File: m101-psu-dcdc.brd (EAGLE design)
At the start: 100 x 50 mm, 39 parts, among them U1 FX2-20P-1.27DS, U2 SHHN000A3CL41Z, U3 G3VM-62C1, U4 ERM1-5MM, U5 SCREW-M2X8, U6 SCREW-M2X8, U7 NUT-M2-SELFLOCK, U8 NUT-M2-SELFLOCK

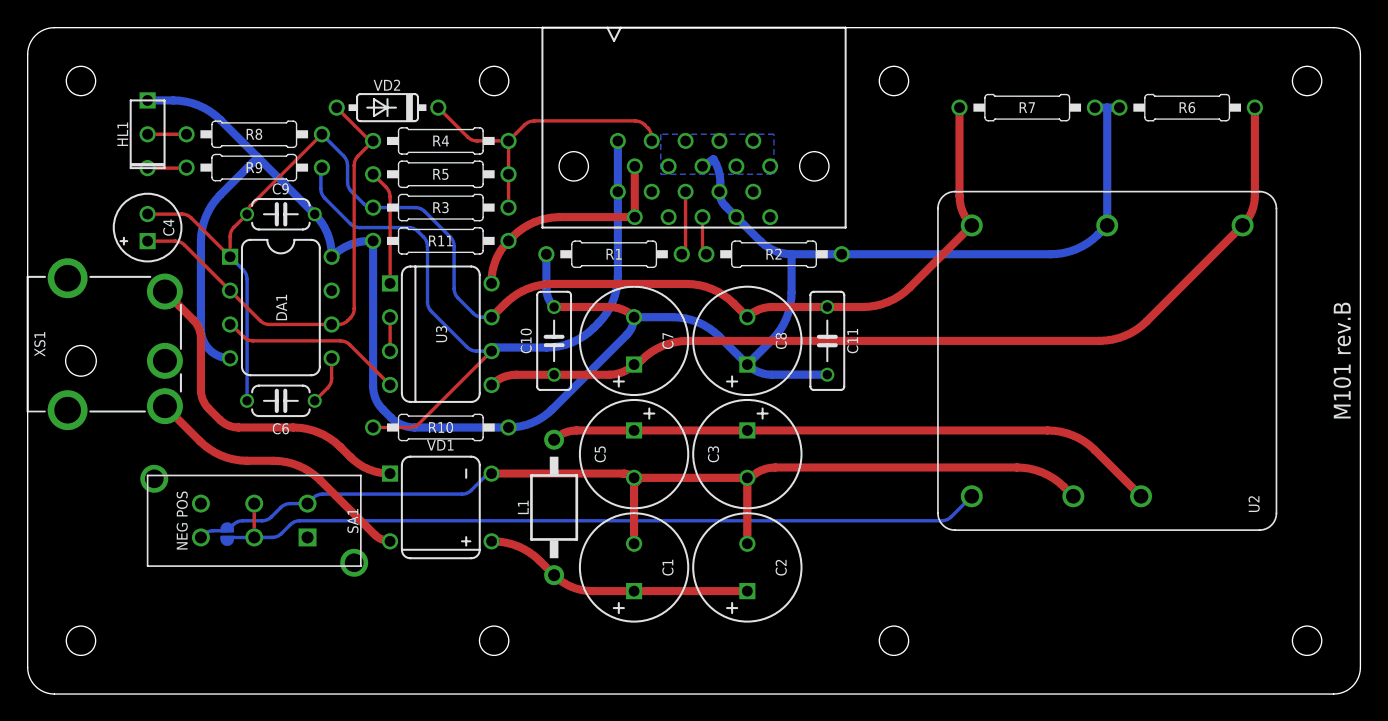
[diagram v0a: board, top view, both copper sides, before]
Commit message: M101 rev.C Initial Schematic
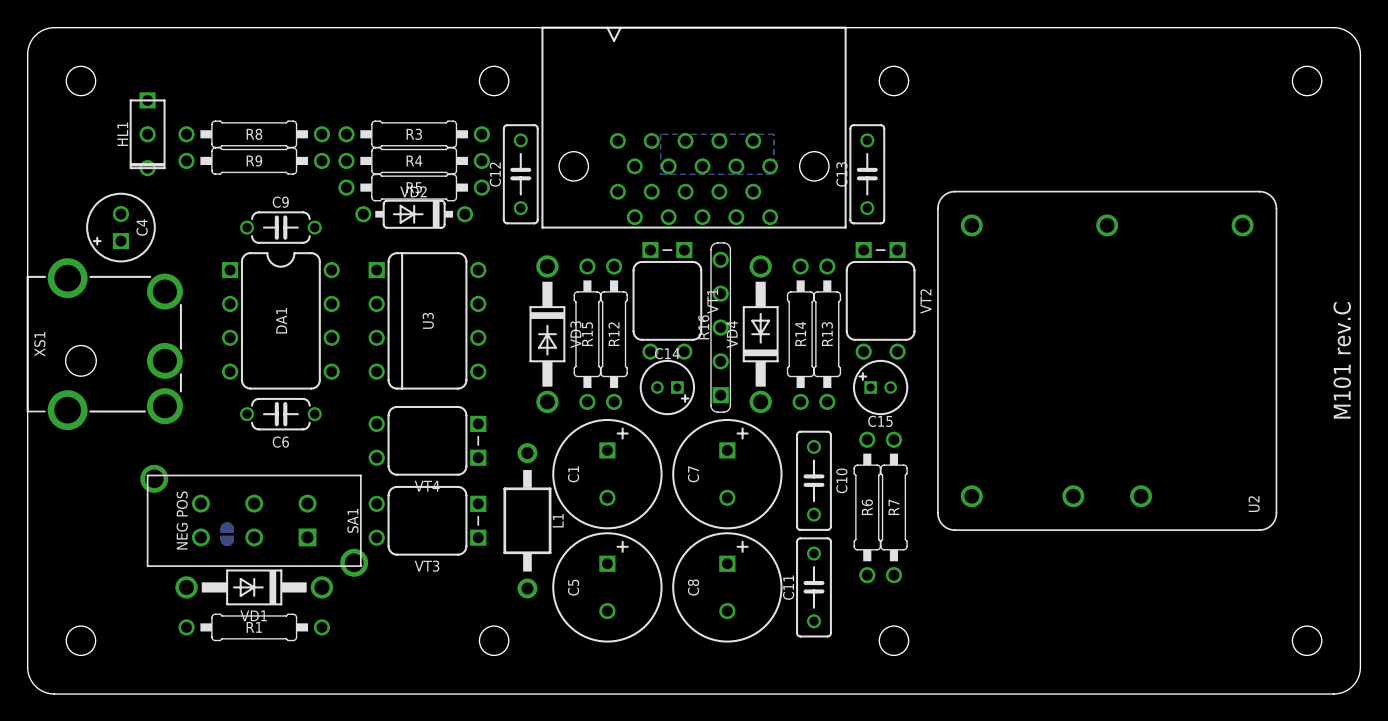
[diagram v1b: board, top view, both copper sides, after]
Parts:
- removed C2, C3: 33U/50V, capacitors-electrolytic:E3,5-8
- removed R10, R11, R2: 100K(TH), resistors:R-0207/10
- added C12, C13: 22N(FILM), capacitors:C050-025X075
- added C14, C15: 1U/50V, capacitors-electrolytic:E1,5-4
- added R12, R13: 100R(TH), resistors:R-0207/10
- added R14, R15: 220K(TH), resistors:R-0207/10
- added R16: 100K*4(SIL5), resistors:R-SIL5
- added VD3, VD4: 10V(1N4740), diodes-zener:DO41-10
- added VT1: IRFD9024, transistors-fet:HVMDIP-4
- added VT2, VT3, VT4: IRFD014, transistors-fet:HVMDIP-4
- PCB1: value M101 rev.B -> M101 rev.C
- R1: value 100K(TH) -> 22K(TH)
- VD1: value DF01M -> 10V(1N4740); device diodes:MDIP-4 -> diodes-zener:DO41-10
- moved R1 38.9 mm to (17.0, 5.00), turned to 0 degrees
- moved R6 38.4 mm to (63.0, 14.0), turned to 90 degrees
- moved R7 31.6 mm to (65.0, 14.0), turned to 90 degrees
- moved C10 22.1 mm to (59.0, 16.0), turned to 90 degrees
- moved C8 18.6 mm to (52.5, 8.00), turned to 270 degrees
- moved C11 18.5 mm to (59.0, 8.00), turned to 90 degrees
- moved VD1 15.2 mm to (17.0, 8.00), turned to 180 degrees
- moved C7 12.2 mm to (52.5, 16.5), turned to 270 degrees
- moved C5 10.2 mm to (43.5, 8.00)
- moved VD2 8.25 mm to (29.0, 36.0)
- moved C1 7.28 mm to (43.5, 16.5), turned to 270 degrees
- moved R3 5.85 mm to (29.0, 42.0)
- moved R4 2.50 mm to (29.0, 40.0)
- moved L1 2.24 mm to (37.5, 13.0), turned to 270 degrees
- moved R5 2.24 mm to (29.0, 38.0)
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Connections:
- removed net N$2: VD1.1, XS1.3
- new net N$17: C14.-, R12.1, R15.1, VD3.A, VT1.3
- new net N$18: C12.2, PCB1.A+15', PCB1.B+15', VT1.1, VT1.2
- new net N$19: C12.1, R12.2
- new net N$21: C13.1, PCB1.A-15', PCB1.B-15', VT2.1, VT2.2
- new net N$23: C13.2, R13.2
- new net N$24: C15.+, R13.1, R14.1, VD4.C, VT2.3
- new net N$25: C15.-, R16.3, U3.8, VD4.A, VT2.4
- net GND: now also R14.2, R15.2, R16.1; no longer R1.2, R10.1, R11.2, R2.2
- net N$11: now also C14.+, R16.2, R9.2, U3.6, VD3.C, VT1.4; no longer VD1.2, XS1.1
- net N$12: now also R1.2, VD1.C, VT3.3, VT4.3; no longer PCB1.A-15', PCB1.B-15', R11.1, U3.8
- net N$20: now also R1.1, XS1.3; no longer C2.+, VD1.3
- net N$22: no longer C3.+
- net N$3: now also VD1.A, VT3.1, VT3.2, VT4.1, VT4.2; no longer C2.-, C3.-, VD1.4
- net N$4: now also R16.4; no longer R1.1
- net N$5: now also R16.5; no longer R2.1
- net N$8: now also VT3.4, VT4.4, XS1.1; no longer PCB1.A+15', PCB1.B+15', R10.2, R9.2, U3.6
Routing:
- net GND: track 156.8 -> 0.00 mm
- net -15V: track 101.0 -> 0.00 mm
- net N$3: track 78.0 -> 0.00 mm
- net N$15: track 69.3 -> 0.00 mm
- net N$16: track 59.5 -> 0.00 mm
- net N$8: track 56.0 -> 0.00 mm
- net N$22: track 45.9 -> 0.00 mm
- net N$10: track 35.4 -> 0.00 mm
- net N$2: track 24.8 -> 0.00 mm
- net SENSE: track 23.4 -> 0.00 mm
- net N$11: track 20.4 -> 0.00 mm
- net N$20: track 20.2 -> 0.00 mm
- net N$12: track 17.2 -> 0.00 mm
- net N$7: track 13.8 -> 0.00 mm
- net N$1: track 8.65 -> 0.00 mm
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
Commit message: M101 Parts renumbering
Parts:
- removed C14, C15: 1U/50V, capacitors-electrolytic:E1,5-4
- added C2: 10U/35V, capacitors-electrolytic:E2-5
- added C3: 33U/50V, capacitors-electrolytic:E3,5-8
- C10, C11: value 100N(FILM) -> 1U/50V; device capacitors:C050-025X075 -> capacitors-electrolytic:E1,5-4
- C4: value 10U/35V -> 100N(TH); device capacitors-electrolytic:E2-5 -> capacitors:C050-024X044
- C5: value 33U/50V -> 39U/35V
- C6: value 100N(TH) -> 39U/35V; device capacitors:C050-024X044 -> capacitors-electrolytic:E3,5-8
- C7: value 39U/35V -> 100N(TH); device capacitors-electrolytic:E3,5-8 -> capacitors:C050-024X044
- C8: value 39U/35V -> 100N(FILM); device capacitors-electrolytic:E3,5-8 -> capacitors:C050-025X075
- C9: value 100N(TH) -> 100N(FILM); device capacitors:C050-024X044 -> capacitors:C050-025X075
- U1: value FX2-20P-1.27DS -> SCREW-M2X8
- U2: value SHHN000A3CL41Z -> SCREW-M2X8; device regulators-switch-mode:DC/DC-C1 -> hardware:EMPTY
- U3: value G3VM-62C1 -> NUT-M2-SELFLOCK; device optoelectronics:DIL08 -> hardware:EMPTY
- U4: value ERM1-5MM -> NUT-M2-SELFLOCK
- U5: value SCREW-M2X8 -> FX2-20P-1.27DS
- U6: value SCREW-M2X8 -> SHHN000A3CL41Z; device hardware:EMPTY -> regulators-switch-mode:DC/DC-C1
- U7: value NUT-M2-SELFLOCK -> G3VM-62C1; device hardware:EMPTY -> optoelectronics:DIL08
- U8: value NUT-M2-SELFLOCK -> ERM1-5MM
- VT1: value IRFD9024 -> IRFD014
- VT3: value IRFD014 -> IRFD9024
- moved U2 210.1 mm to (-84.0, -105.0), turned to 0 degrees
- moved U6 210.1 mm to (81.0, 25.0), turned to 90 degrees
- moved U3 177.3 mm to (-85.0, -107.0), turned to 0 degrees
- moved U7 177.3 mm to (30.0, 28.0), turned to 270 degrees
- moved C9 48.3 mm to (59.0, 8.00), turned to 90 degrees
- moved C7 38.3 mm to (19.0, 35.0), turned to 0 degrees
- moved VT2 37.8 mm to (30.0, 13.0), turned to 90 degrees
- moved C6 35.9 mm to (52.5, 8.00), turned to 270 degrees
- moved VT4 35.6 mm to (64.0, 29.5), turned to 180 degrees
- moved VT3 24.4 mm to (48.0, 29.5), turned to 180 degrees
- moved VT1 20.8 mm to (30.0, 19.0), turned to 90 degrees
- moved C4 18.4 mm to (19.0, 21.0), turned to 0 degrees
- moved C11 15.8 mm to (64.0, 23.0), turned to 0 degrees
- moved C10 13.0 mm to (48.0, 23.0), turned to 180 degrees
- moved C5 12.4 mm to (52.5, 16.5)
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- renumbered R14 to R11, R15 to R10, R16 to R2
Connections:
- net -15V: now also C2.-, C4.1, C6.-, C7.1, U6.6, U7.7; no longer C11.1, C4.-, C6.1, C8.-, U2.6, U3.7
- net GND: now also C5.-, C6.+, C7.2, C8.1, U6.5; no longer C10.1, C11.2, C7.-, C8.+, U2.5
- net N$1: now also U7.1; no longer U3.1
- net N$10: now also C2.+; no longer C4.+
- net N$11: now also C10.+, U7.6, VT3.4; no longer C14.+, U3.6, VT1.4
- net N$12: now also VT1.3, VT2.3; no longer VT3.3, VT4.3
- net N$15: now also C5.+, C8.2, U6.4, U7.5; no longer C10.2, C7.+, U2.4, U3.5
- net N$16: now also U6.3; no longer U2.3
- net N$17: now also C10.-, VT3.3; no longer C14.-, VT1.3
- net N$18: now also VT3.1, VT3.2; no longer VT1.1, VT1.2
- net N$21: now also VT4.1, VT4.2; no longer VT2.1, VT2.2
- net N$22: now also C3.+, U6.1; no longer C5.+, U2.1
- net N$24: now also C11.+, VT4.3; no longer C15.+, VT2.3
- net N$25: now also C11.-, U7.8, VT4.4; no longer C15.-, U3.8, VT2.4
- net N$3: now also C3.-, U6.2, VT1.1, VT1.2, VT2.1, VT2.2; no longer C5.-, U2.2, VT3.1, VT3.2, VT4.1, VT4.2
- net N$6: now also C4.2; no longer C6.2
- net N$7: now also U7.4; no longer U3.4
- net N$8: now also VT1.4, VT2.4; no longer VT3.4, VT4.4
- net N$9: now also U7.2, U7.3; no longer U3.2, U3.3

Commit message: M101 Polarity Protection Fix
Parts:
- turned VT1 to 270 degrees
- turned VT2 to 270 degrees
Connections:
- net N$3: now also VT1.4, VT2.4; no longer VT1.1, VT1.2, VT2.1, VT2.2
- net N$8: now also VT1.1, VT1.2, VT2.1, VT2.2; no longer VT1.4, VT2.4
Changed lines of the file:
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@@
 <?xml version="1.0" encoding="utf-8"?>
 <!DOCTYPE eagle SYSTEM "eagle.dtd">
-<eagle version="7.5.4">
+<eagle version="7.6.0">
 <drawing>
 <settings>
@@
 <attribute name="MOUSER" value="652-4605X-1LF-100K" x="52" y="27.5" size="1.778" layer="27" rot="R90" display="off"/>
 </element>
-<element name="VT2" library="transistors-fet" package="HVMDIP-4" value="IRFD014" x="30" y="13" rot="R90"/>
-<element name="VT1" library="transistors-fet" package="HVMDIP-4" value="IRFD014" x="30" y="19" rot="R90"/>
+<element name="VT2" library="transistors-fet" package="HVMDIP-4" value="IRFD014" x="30" y="13" rot="R270"/>
+<element name="VT1" library="transistors-fet" package="HVMDIP-4" value="IRFD014" x="30" y="19" rot="R270"/>
 <element name="VD1" library="diodes-zener" package="DO41-10" value="10V(1N4740)" x="17" y="8" rot="R180"/>
 <element name="R1" library="resistors" package="R-0207/10" value="22K(TH)" x="17" y="5">
@@
 <contactref element="C1" pad="-"/>
 <contactref element="S1" pad="1"/>
-<contactref element="VT2" pad="1"/>
-<contactref element="VT2" pad="2"/>
-<contactref element="VT1" pad="1"/>
-<contactref element="VT1" pad="2"/>
 <contactref element="VD1" pad="A"/>
+<contactref element="VT1" pad="4"/>
+<contactref element="VT2" pad="4"/>
 <wire x1="43.5" y1="14.722" x2="78.46" y2="14.84" width="0" layer="19" extent="1-1"/>
 <wire x1="43.5" y1="6.222" x2="43.5" y2="14.722" width="0" layer="19" extent="1-1"/>
-<wire x1="33.81" y1="17.73" x2="43.5" y2="14.722" width="0" layer="19" extent="1-1"/>
-<wire x1="33.81" y1="20.27" x2="33.81" y2="17.73" width="0" layer="19" extent="1-1"/>
-<wire x1="33.81" y1="14.27" x2="33.81" y2="17.73" width="0" layer="19" extent="1-1"/>
-<wire x1="33.81" y1="11.73" x2="33.81" y2="14.27" width="0" layer="19" extent="1-1"/>
-<wire x1="21" y1="14.29" x2="33.81" y2="17.73" width="0" layer="19" extent="1-1"/>
+<wire x1="33.81" y1="14.27" x2="43.5" y2="14.722" width="0" layer="19" extent="1-1"/>
+<wire x1="33.81" y1="20.27" x2="33.81" y2="14.27" width="0" layer="19" extent="1-1"/>
+<wire x1="21" y1="14.29" x2="33.81" y2="14.27" width="0" layer="19" extent="1-1"/>
 <wire x1="14.974" y1="12.254" x2="21" y2="14.29" width="0" layer="19" extent="16-16"/>
 <wire x1="13" y1="11.75" x2="14.974" y2="12.254" width="0" layer="19" extent="16-16"/>
@@
 </signal>
 <signal name="N$8">
-<contactref element="VT2" pad="4"/>
-<contactref element="VT1" pad="4"/>
 <contactref element="XS1" pad="1"/>
-<wire x1="26.19" y1="11.73" x2="26.19" y2="17.73" width="0" layer="19" extent="1-1"/>
-<wire x1="10.3" y1="21.6" x2="26.19" y2="17.73" width="0" layer="19" extent="1-1"/>
+<contactref element="VT1" pad="1"/>
+<contactref element="VT1" pad="2"/>
+<contactref element="VT2" pad="1"/>
+<contactref element="VT2" pad="2"/>
+<wire x1="26.19" y1="17.73" x2="26.19" y2="20.27" width="0" layer="19" extent="1-1"/>
+<wire x1="26.19" y1="14.27" x2="26.19" y2="17.73" width="0" layer="19" extent="1-1"/>
+<wire x1="26.19" y1="11.73" x2="26.19" y2="14.27" width="0" layer="19" extent="1-1"/>
+<wire x1="10.3" y1="21.6" x2="26.19" y2="20.27" width="0" layer="19" extent="1-1"/>
 </signal>
 <signal name="N$12">
@@
 <contactref element="VD1" pad="C"/>
 <contactref element="R1" pad="2"/>
-<wire x1="26.19" y1="14.27" x2="26.19" y2="20.27" width="0" layer="19" extent="1-1"/>
-<wire x1="22.08" y1="8" x2="26.19" y2="14.27" width="0" layer="19" extent="1-1"/>
+<wire x1="33.81" y1="11.73" x2="33.81" y2="17.73" width="0" layer="19" extent="1-1"/>
+<wire x1="22.08" y1="8" x2="33.81" y2="11.73" width="0" layer="19" extent="1-1"/>
 <wire x1="22.08" y1="5" x2="22.08" y2="8" width="0" layer="19" extent="1-1"/>
 </signal>

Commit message: M101c Update
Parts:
- moved C10 1.00 mm to (48.0, 22.0)
- moved C11 1.00 mm to (64.0, 22.0)
- moved R10 1.00 mm to (42.0, 28.0)
- moved R11 1.00 mm to (58.0, 28.0)
- moved R12 1.00 mm to (44.0, 28.0)
- moved R13 1.00 mm to (60.0, 28.0)
- moved R6 1.00 mm to (63.0, 13.0)
- moved R7 1.00 mm to (65.0, 13.0)
- moved VD3 1.00 mm to (39.0, 28.0)
- moved VD4 1.00 mm to (55.0, 28.0)
- moved VT3 1.00 mm to (48.0, 28.5)
- moved VT4 1.00 mm to (64.0, 28.5)

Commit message: M101c: Routing
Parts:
- moved C5 8.50 mm to (52.5, 8.00), turned to 90 degrees
- moved C6 8.50 mm to (52.5, 16.5), turned to 90 degrees
- moved C8 8.00 mm to (59.0, 8.00), turned to 270 degrees
- moved C9 8.00 mm to (59.0, 16.0), turned to 270 degrees
- moved R6 2.00 mm to (65.0, 13.0), turned to 270 degrees
- moved R7 2.00 mm to (63.0, 13.0), turned to 270 degrees
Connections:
- new net N$2: XS1.2
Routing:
- net -15V: track 0.00 -> 116.0 mm
- net N$3: track 0.00 -> 113.9 mm
- net GND: track 0.00 -> 96.0 mm
- net N$15: track 0.00 -> 95.0 mm
- net N$20: track 0.00 -> 74.4 mm
- net N$16: track 0.00 -> 59.9 mm
- net N$11: track 0.00 -> 53.7 mm
- net N$22: track 0.00 -> 50.6 mm
- net N$25: track 0.00 -> 44.0 mm
- net N$10: track 0.00 -> 33.1 mm
- net N$21: track 0.00 -> 27.9 mm
- net N$8: track 0.00 -> 27.0 mm
- net N$12: track 0.00 -> 23.7 mm
- net N$23: track 0.00 -> 20.9 mm
- net SENSE: track 0.00 -> 20.4 mm
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- added copper zone on layer 1, net GND

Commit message: M101d Schematic/Routing Update
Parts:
- PCB1: value M101 rev.C -> M101 rev.D
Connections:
- net N$20: now also XS1.1; no longer XS1.3
- net N$8: now also XS1.3; no longer XS1.1
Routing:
- net N$20: track 74.4 -> 60.8 mm
- net N$8: track 27.0 -> 39.2 mm
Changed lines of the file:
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@@
 <attribute name="MOUSER" value="894-SHHN000A3CL41Z" x="81" y="25" size="1.778" layer="27" rot="R90" display="off"/>
 </element>
-<element name="PCB1" library="module-footprints" package="ST2-BOARD-50-PSU" value="M101 rev.C" x="0" y="0"/>
+<element name="PCB1" library="module-footprints" package="ST2-BOARD-50-PSU" value="M101 rev.D" x="0" y="0"/>
 <element name="XS1" library="connectors" package="PJ-051AH" value="PJ-051AH" x="0" y="25">
 <attribute name="MOUSER" value="490-PJ-051AH" x="0" y="25" size="1.778" layer="27" display="off"/>
@@
 <contactref element="L1" pad="1"/>
 <contactref element="C1" pad="+"/>
-<contactref element="XS1" pad="3"/>
 <contactref element="R1" pad="1"/>
 <wire x1="37.5" y1="18.08" x2="37.5" y2="18.5857875" width="0.4064" layer="16"/>
@@
 <wire x1="24.70710625" y1="21.70710625" x2="22.29289375" y2="19.29289375" width="0.4064" layer="16"/>
 <wire x1="22.29289375" y1="19.29289375" x2="21.5857875" y2="19" width="0.4064" layer="16" curve="-45"/>
-<wire x1="21.5857875" y1="19" x2="14.4142125" y2="19" width="0.4064" layer="16"/>
-<wire x1="14.4142125" y1="19" x2="13.70710625" y2="19.29289375" width="0.4064" layer="16" curve="-45"/>
-<wire x1="13.70710625" y1="19.29289375" x2="12.79289375" y2="20.20710625" width="0.4064" layer="16"/>
-<wire x1="12.79289375" y1="20.20710625" x2="12.5" y2="20.9142125" width="0.4064" layer="16" curve="-45"/>
-<wire x1="12.5" y1="20.9142125" x2="12.5" y2="27.5857875" width="0.4064" layer="16"/>
-<wire x1="12.5" y1="27.5857875" x2="12.20710625" y2="28.29289375" width="0.4064" layer="16" curve="45"/>
-<wire x1="12.20710625" y1="28.29289375" x2="10.3" y2="30.2" width="0.4064" layer="16"/>
-<wire x1="11.92" y1="5" x2="10.4142125" y2="5" width="0.254" layer="16"/>
-<wire x1="10.4142125" y1="5" x2="9.70710625" y2="5.29289375" width="0.254" layer="16" curve="-45"/>
-<wire x1="9.70710625" y1="5.29289375" x2="7.79289375" y2="7.20710625" width="0.254" layer="16"/>
-<wire x1="7.79289375" y1="7.20710625" x2="7.5" y2="7.9142125" width="0.254" layer="16" curve="-45"/>
-<wire x1="7.5" y1="7.9142125" x2="7.5" y2="26.9857875" width="0.254" layer="16"/>
-<wire x1="7.5" y1="26.9857875" x2="7.79289375" y2="27.69289375" width="0.254" layer="16" curve="-45"/>
-<wire x1="7.79289375" y1="27.69289375" x2="10.3" y2="30.2" width="0.254" layer="16"/>
+<wire x1="21.5857875" y1="19" x2="13.3142125" y2="19" width="0.4064" layer="16"/>
+<wire x1="13.3142125" y1="19" x2="12.60710625" y2="19.29289375" width="0.4064" layer="16" curve="-45"/>
+<wire x1="12.60710625" y1="19.29289375" x2="10.3" y2="21.6" width="0.4064" layer="16"/>
 <wire x1="37.5" y1="18.08" x2="43.302" y2="18.08" width="0.4064" layer="16"/>
 <wire x1="43.302" y1="18.08" x2="43.5" y2="18.278" width="0.4064" layer="16"/>
+<contactref element="XS1" pad="1"/>
+<wire x1="11.92" y1="5" x2="8.4142125" y2="5" width="0.254" layer="1"/>
+<wire x1="8.4142125" y1="5" x2="7.70710625" y2="5.29289375" width="0.254" layer="1" curve="-45"/>
+<wire x1="7.70710625" y1="5.29289375" x2="7.29289375" y2="5.70710625" width="0.254" layer="1"/>
+<wire x1="7.29289375" y1="5.70710625" x2="7" y2="6.4142125" width="0.254" layer="1" curve="-45"/>
+<wire x1="7" y1="6.4142125" x2="7" y2="20.0857875" width="0.254" layer="1"/>
+<wire x1="7" y1="20.0857875" x2="7.29289375" y2="20.79289375" width="0.254" layer="1" curve="-45"/>
+<wire x1="7.29289375" y1="20.79289375" x2="7.70710625" y2="21.20710625" width="0.254" layer="1"/>
+<wire x1="7.70710625" y1="21.20710625" x2="8.4142125" y2="21.5" width="0.254" layer="1" curve="-45"/>
+<wire x1="8.4142125" y1="21.5" x2="10.2" y2="21.5" width="0.254" layer="1"/>
+<wire x1="10.2" y1="21.5" x2="10.3" y2="21.6" width="0.254" layer="1"/>
 </signal>
 <signal name="N$22" class="1">
@@
 </signal>
 <signal name="N$8" class="1">
-<contactref element="XS1" pad="1"/>
 <contactref element="VT1" pad="1"/>
 <contactref element="VT1" pad="2"/>
 <contactref element="VT2" pad="1"/>
 <contactref element="VT2" pad="2"/>
-<wire x1="10.3" y1="21.6" x2="10.3" y2="20.1142125" width="0.4064" layer="16"/>
-<wire x1="10.3" y1="20.1142125" x2="10.59289375" y2="19.40710625" width="0.4064" layer="16" curve="45"/>
-<wire x1="10.59289375" y1="19.40710625" x2="11.70710625" y2="18.29289375" width="0.4064" layer="16"/>
-<wire x1="11.70710625" y1="18.29289375" x2="12.4142125" y2="18" width="0.4064" layer="16" curve="45"/>
-<wire x1="12.4142125" y1="18" x2="25.92" y2="18" width="0.4064" layer="16"/>
+<wire x1="25.92" y1="18" x2="9.4142125" y2="18" width="0.4064" layer="16"/>
+<wire x1="9.4142125" y1="18" x2="8.70710625" y2="18.29289375" width="0.4064" layer="16" curve="-45"/>
+<wire x1="8.70710625" y1="18.29289375" x2="8.29289375" y2="18.70710625" width="0.4064" layer="16"/>
+<wire x1="8.29289375" y1="18.70710625" x2="8" y2="19.4142125" width="0.4064" layer="16" curve="-45"/>
+<wire x1="8" y1="19.4142125" x2="8" y2="27.4857875" width="0.4064" layer="16"/>
 <wire x1="25.92" y1="18" x2="26.19" y2="17.73" width="0.4064" layer="16"/>
 <wire x1="26.19" y1="20.27" x2="26.19" y2="17.73" width="0.4064" layer="16"/>
 <wire x1="26.19" y1="17.73" x2="26.19" y2="14.27" width="0.4064" layer="16"/>
 <wire x1="26.19" y1="11.73" x2="26.19" y2="14.27" width="0.4064" layer="16"/>
+<contactref element="XS1" pad="3"/>
+<wire x1="8" y1="27.4857875" x2="8.29289375" y2="28.19289375" width="0.4064" layer="16" curve="-45"/>
+<wire x1="8.29289375" y1="28.19289375" x2="10.3" y2="30.2" width="0.4064" layer="16"/>
 </signal>
 <signal name="N$12" class="1">
